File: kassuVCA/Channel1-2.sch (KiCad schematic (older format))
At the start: 62 parts, among them Q401 MBT3904DW1, Q402 MBT3904DW1, Q403 MBT3904DW1, SW401 SW_DPDT_x2, SW402 SW_DPDT_x2, U401 TL074

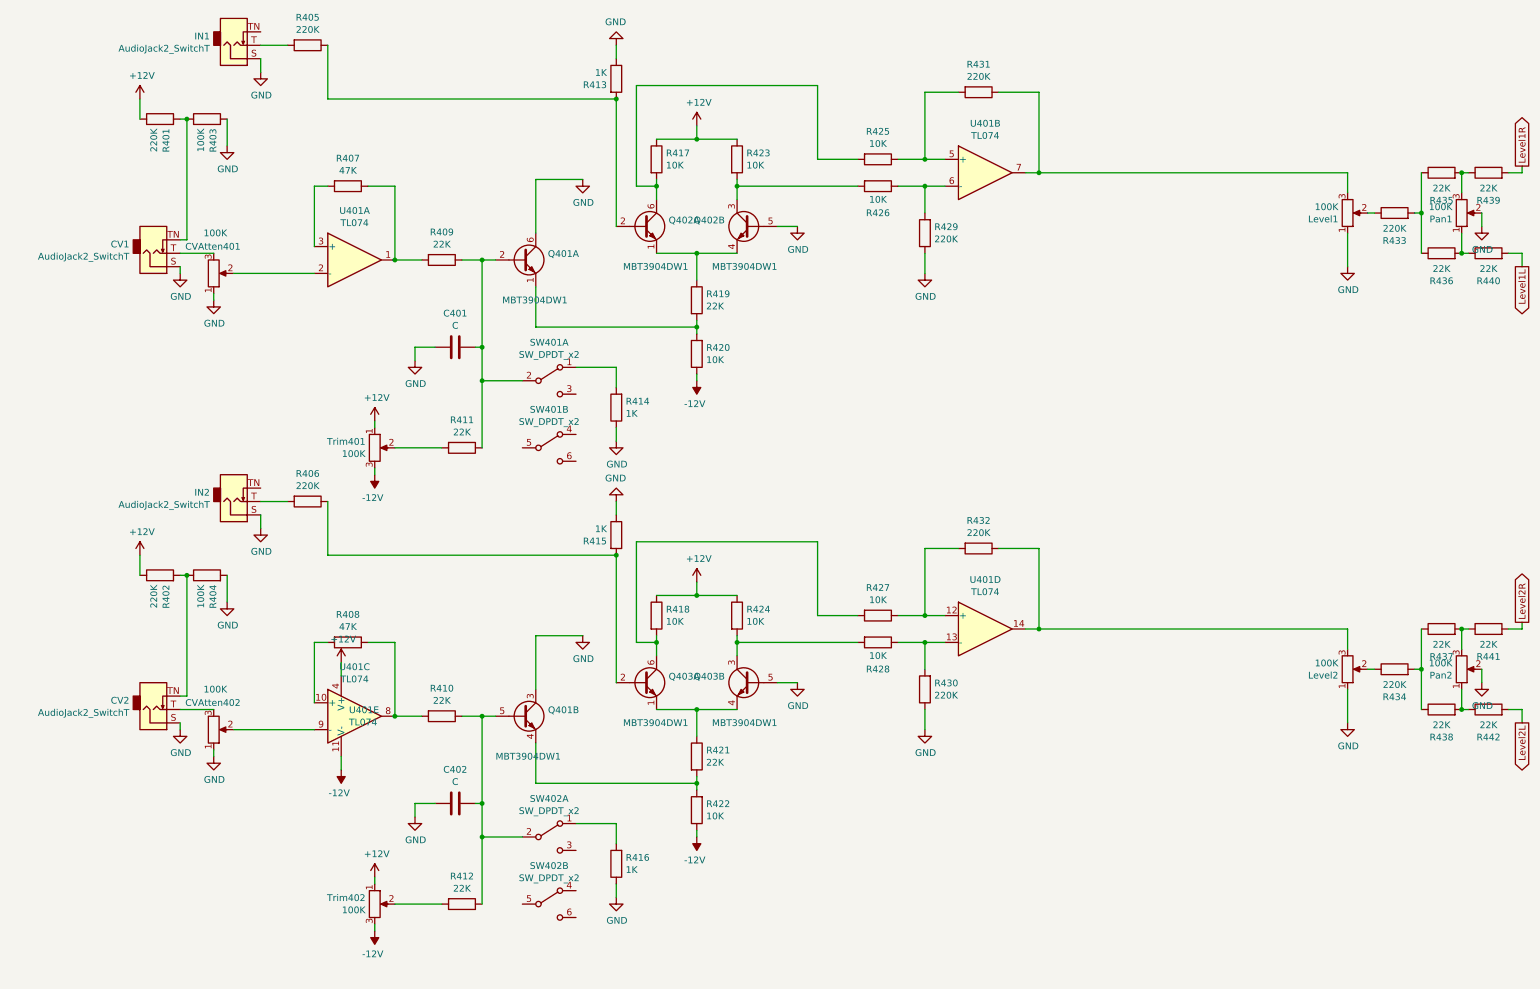
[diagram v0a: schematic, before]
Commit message: WIP 0805 TL072 dual channel
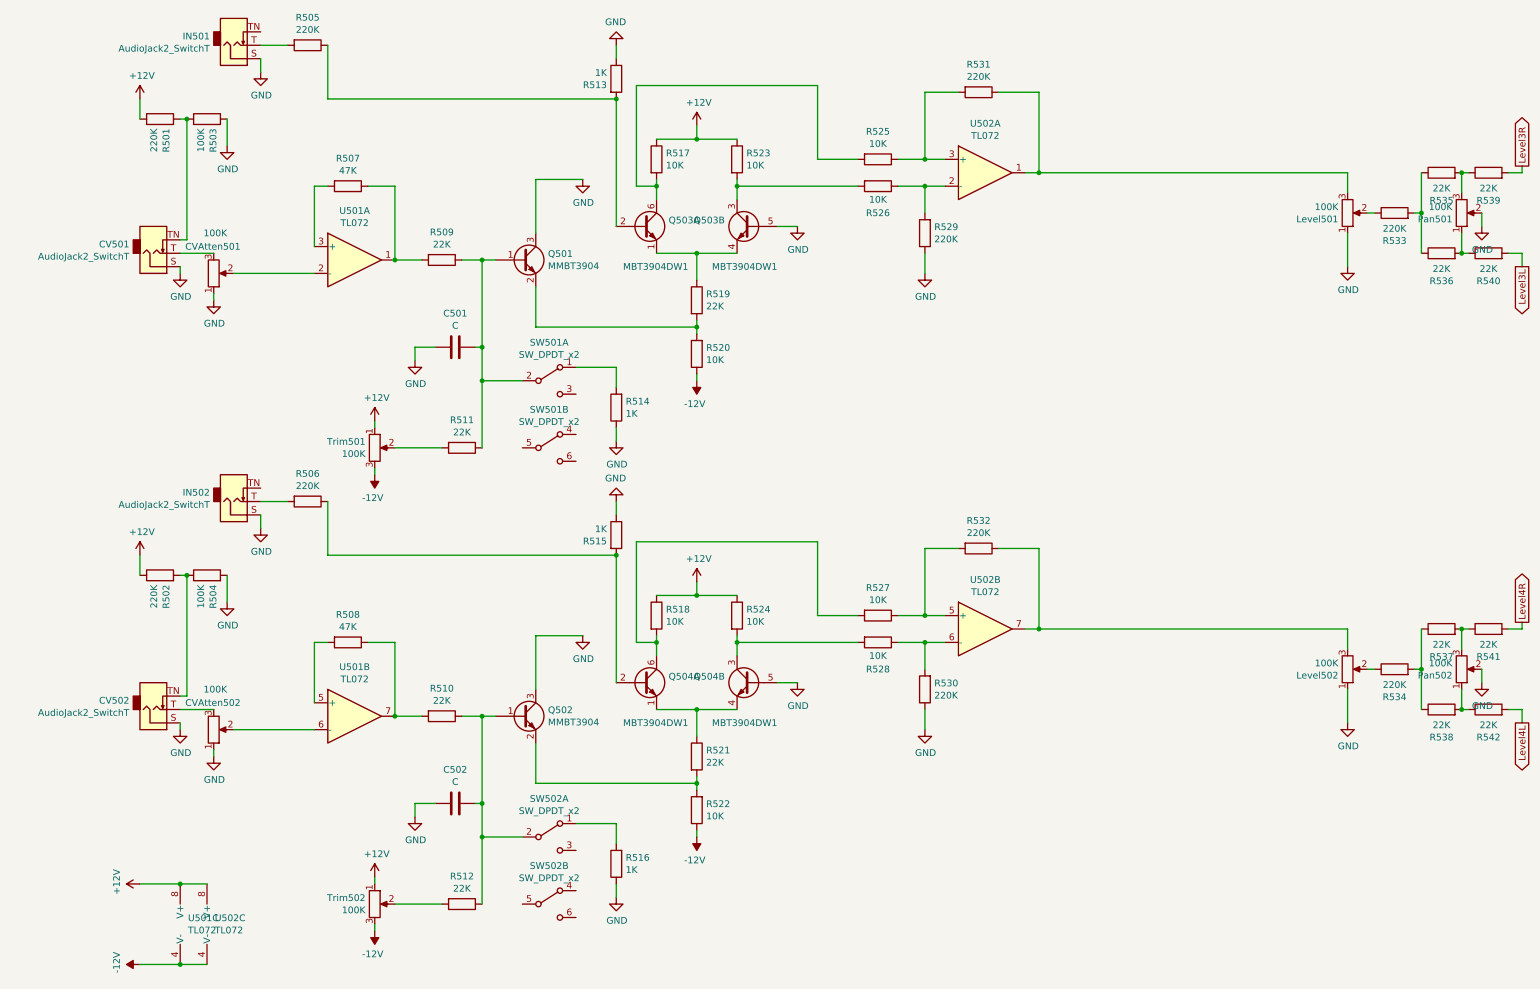
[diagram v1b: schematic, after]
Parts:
- removed Q401: MBT3904DW1, Package_TO_SOT_SMD:SOT-363_SC-70-6, symbol Transistor_BJT:MBT3904DW1
- removed U401: TL074, Package_SO:SOIC-14_3.9x8.7mm_P1.27mm, symbol Amplifier_Operational:TL074
- added Q401, Q404: MMBT3904, Package_TO_SOT_SMD:SOT-23, symbol Transistor_BJT:MMBT3904
- added U401, U402: TL072, Package_SO:SOIC-8_3.9x4.9mm_P1.27mm, symbol Amplifier_Operational:TL072
- R401, R402, R403, R404, R405, R406, R407, R408, R409, R410, R411, R412, R413, R414, R415, R416, R417, R418, R419, R420, R421, R422, R423, R424, R425, R426, R427, R428, R429, R430, R431, R432, R433, R434, R435, R436, R437, R438, R439, R440, R441, R442: footprint Resistor_THT:R_Axial_DIN0207_L6.3mm_D2.5mm_P7.62mm_Horizontal -> Resistor_SMD:R_0805_2012Metric_Pad1.20x1.40mm_HandSolder
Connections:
- net +12V: now also U401.8 (V+), U402.8 (V+)
- net -12V: now also U401.4 (V-), U402.4 (V-)
- net GND: now also Q401.3 (C), Q404.3 (C)
- net at R425.1, R431.2: now also U402.3 (+)
- net at R426.1, R429.2: now also U402.2 (-)
- net at CVAtten401.2: now also U401.2 (-)
- net at C401.1, R409.1, R411.1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: now also Q401.1 (B)
- net at R407.1, R409.2: now also U401.1
- net at Level1.3, R431.1: now also U402.1
- net at R419.2, R420.2: now also Q401.2 (E)
- net at R407.2: now also U401.3 (+)
- net at R421.2, R422.2: now also Q404.2 (E)
- net at R427.1, R432.2: now also U402.5 (+)
- net at R428.1, R430.2: now also U402.6 (-)
- net at Level2.3, R432.1: now also U402.7
- net at C402.1, R410.1, R412.1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: now also Q404.1 (B)
- net at CVAtten402.2: now also U401.6 (-)
- net at R408.1, R410.2: now also U401.7
- net at R408.2: now also U401.5 (+)
- net Level1L renamed Level3L
- net Level1R renamed Level3R
- net Level2L renamed Level4L
- net Level2R renamed Level4R
